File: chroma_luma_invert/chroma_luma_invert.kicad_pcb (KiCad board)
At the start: 2 copper layers, 100 x 100 mm, 69 parts, among them J1 rca, J2 rca, J3 Barrel_Jack, J4 Conn_01x12, SW1 SPDT, SW2 SPDT, U1 AD8044, U2 LM393, U3 CD4051, U4 LM317, U5 74HC4538, U6 CD4040, U7 74HC4538, U8 74HC4538

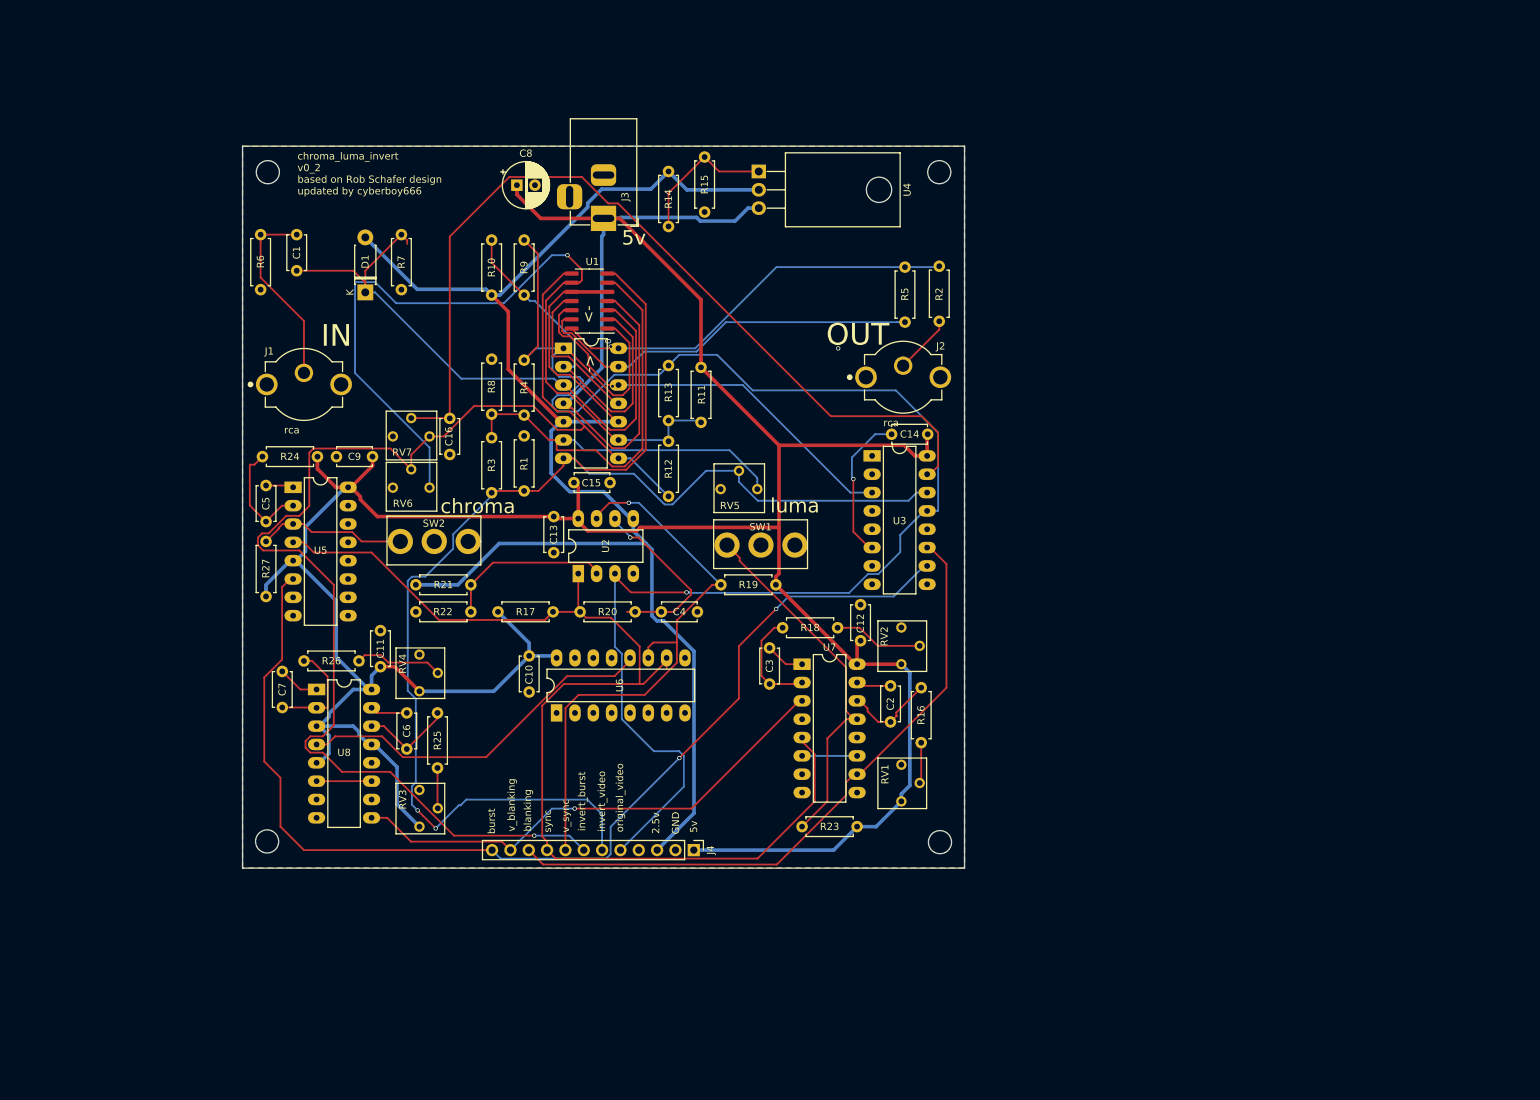
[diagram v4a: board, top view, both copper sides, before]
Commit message: update for new chroma_luma circuit
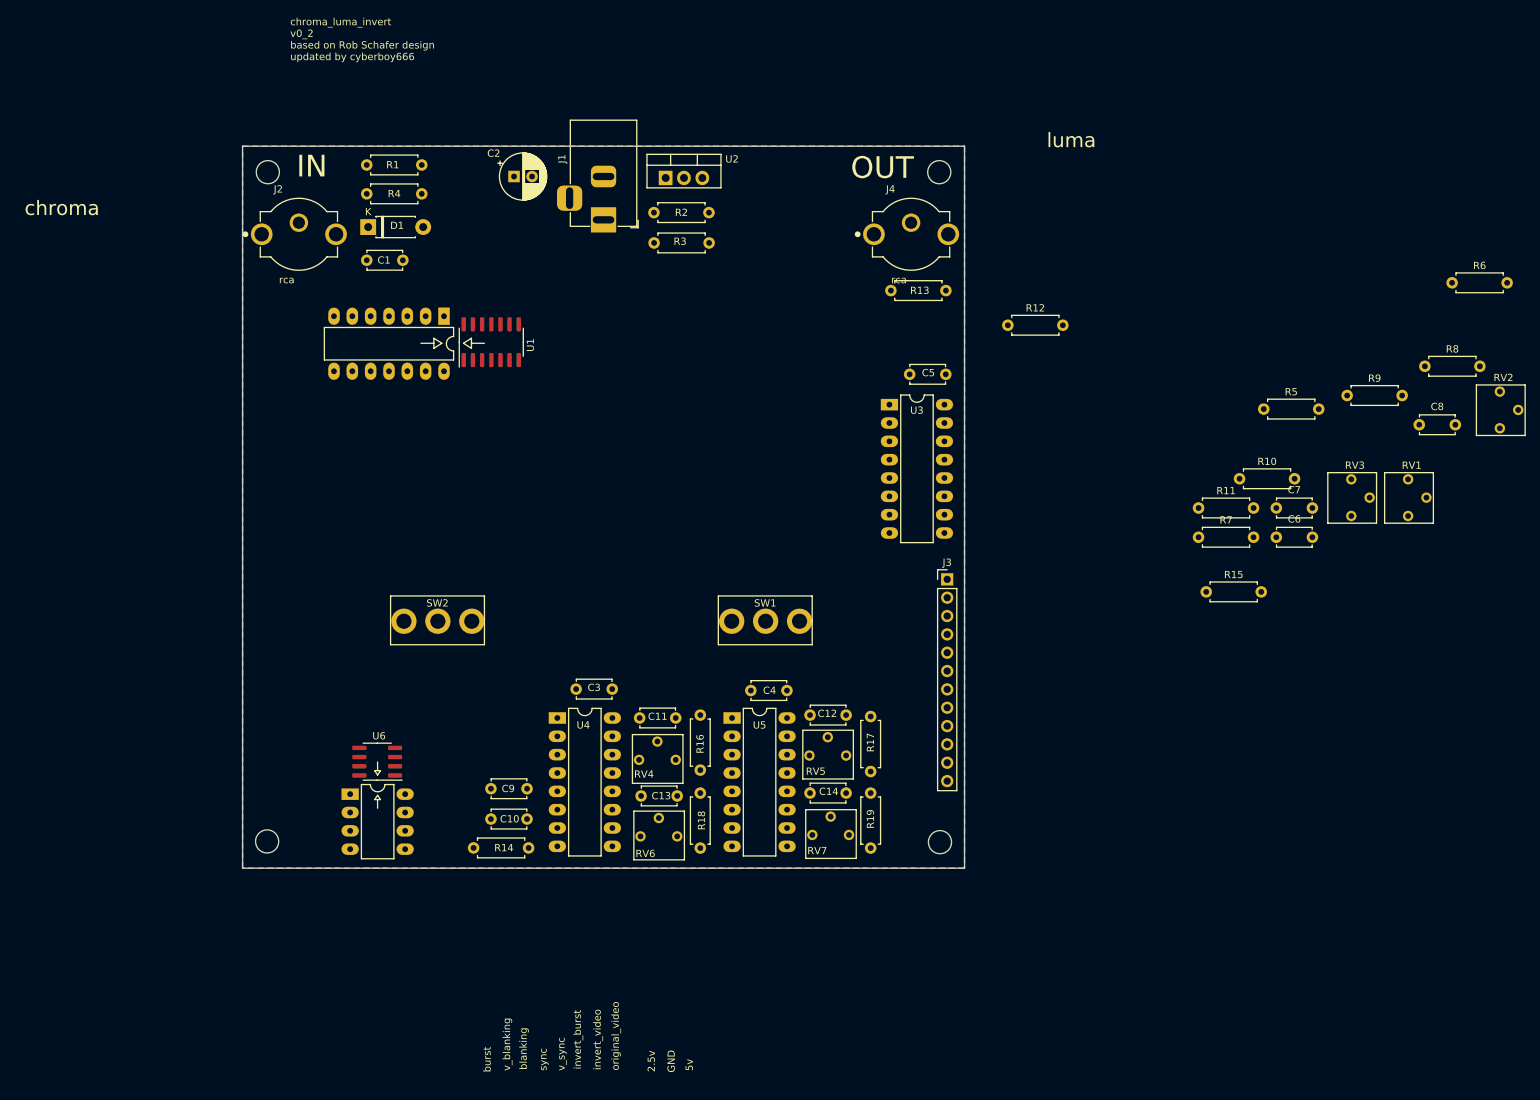
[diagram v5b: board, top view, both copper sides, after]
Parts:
- removed C15: 0.1u, Capacitor_THT:C_Disc_D4.7mm_W2.5mm_P5.00mm
- removed C16: 0.001u, Capacitor_THT:C_Disc_D4.7mm_W2.5mm_P5.00mm
- removed R20, R25: 15k, Resistor_THT:R_Axial_DIN0207_L6.3mm_D2.5mm_P7.62mm_Horizontal
- removed R21: 3.9k, Resistor_THT:R_Axial_DIN0207_L6.3mm_D2.5mm_P7.62mm_Horizontal
- removed R22, R23, R26, R27: 10k, Resistor_THT:R_Axial_DIN0207_L6.3mm_D2.5mm_P7.62mm_Horizontal
- removed R24: 39k, Resistor_THT:R_Axial_DIN0207_L6.3mm_D2.5mm_P7.62mm_Horizontal
- removed U7, U8: 74HC4538, Package_DIP:DIP-16_W7.62mm_LongPads
- C11: value 0.1u -> x1
- C12, C14: value 0.1u -> 0.001u
- C13: value 0.1u -> x2
- C2: value 0.001u -> 10uf; footprint Capacitor_THT:C_Disc_D4.7mm_W2.5mm_P5.00mm -> Capacitor_THT:CP_Radial_D6.3mm_P2.50mm
- C3, C4: value 0.001u -> 0.1u
- C5: value 0.0001u -> 0.1u
- C6, C7: value 0.01u -> 0.1u
- C8: value 10uf -> 0.001u; footprint Capacitor_THT:CP_Radial_D6.3mm_P2.50mm -> Capacitor_THT:C_Disc_D4.7mm_W2.5mm_P5.00mm
- J1: value rca -> Barrel_Jack; footprint lib_fp:tht_vertical_rca -> Connector_BarrelJack:BarrelJack_Horizontal
- J3: value Barrel_Jack -> Conn_01x12; footprint Connector_BarrelJack:BarrelJack_Horizontal -> Connector_PinHeader_2.54mm:PinHeader_1x12_P2.54mm_Vertical
- J4: value Conn_01x12 -> rca; footprint Connector_PinHeader_2.54mm:PinHeader_1x12_P2.54mm_Vertical -> lib_fp:tht_vertical_rca
- R1: value 1.5k -> 75
- R10: value 1k -> 5.6k
- R11: value 5.6k -> 1.5k
- R13: value 1k -> 75
- R14: value 100 -> 680k
- R15: value 100 -> 10k
- R16: value 68k -> y1
- R17: value 1k -> 10k
- R18: value 10k -> y2
- R19: value 1k -> 68k
- R2: value 75 -> 100
- R3: value 1.5k -> 100
- R4: value 1k -> 1m
- R6: value 75 -> 1k
- R7: value 1m -> 1k
- RV1: value 10k_trim -> 1k_trim
- RV2: value 5k_trim -> 1k_trim
- RV3: value 100k_trim -> 1k_trim
- RV4: value 20k_trim -> z1
- RV5: value 1k_trim -> 5k_trim
- RV6: value 1k_trim -> z2
- RV7: value 1k_trim -> 10k_trim
- U1: footprint project_parts:DIP+SOIC_14 -> lib_fp:DIP+SOIC_14
- U2: value LM393 -> LM317; footprint Package_DIP:DIP-8_W7.62mm_LongPads -> Package_TO_SOT_THT:TO-220-3_Vertical
- U4: value LM317 -> 74HC4538; footprint Package_TO_SOT_THT:TO-220-3_Horizontal_TabDown -> Package_DIP:DIP-16_W7.62mm_LongPads
- U6: value CD4040 -> LM1881; footprint Package_DIP:DIP-16_W7.62mm_LongPads -> lib_fp:DIP-SOIC-8
- moved R6 165.2 mm to (272.5, 53.9), turned to 0 degrees
- moved C7 139.5 mm to (248.2, 85.1), turned to 0 degrees
- moved RV3 136.1 mm to (258.6, 86.2)
- moved C8 129.3 mm to (268.0, 73.6)
- moved R8 129.3 mm to (268.8, 65.5), turned to 0 degrees
- moved C6 122.9 mm to (248.2, 89.2), turned to 0 degrees
- moved R7 118.1 mm to (237.4, 89.2), turned to 0 degrees
- moved R9 116.0 mm to (258.0, 69.5), turned to 0 degrees
- moved R10 108.7 mm to (243.1, 81.1), turned to 0 degrees
- moved R14 97.5 mm to (137.0, 132.2), turned to 0 degrees
- moved R15 92.0 mm to (238.5, 96.7), turned to 0 degrees
- moved C5 90.5 mm to (197.4, 66.6), turned to 0 degrees
- moved J4 90.5 mm to (197.6, 47.2), turned to 0 degrees
- moved RV2 89.1 mm to (279.2, 74.1)
- moved C2 87.7 mm to (142.6, 39.2), turned to 0 degrees
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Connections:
- C10 pad 1: GND -> Net-(C10-Pad1)
- C10 pad 2: +5V -> GND
- C11 pad 1: GND -> Net-(C11-Pad1)
- C11 pad 2: +5V -> Net-(C11-Pad2)
- C12 pad 1: GND -> Net-(C12-Pad1)
- C12 pad 2: +5V -> Net-(C12-Pad2)
- C13 pad 1: GND -> Net-(C13-Pad1)
- C13 pad 2: +5V -> Net-(C13-Pad2)
- C14 pad 1: GND -> Net-(C14-Pad1)
- C14 pad 2: +5V -> Net-(C14-Pad2)
- C2 pad 1: Net-(C2-Pad1) -> +5V
- C2 pad 2: Net-(C2-Pad2) -> GND
- C3 pad 1: Net-(C3-Pad1) -> GND
- C3 pad 2: Net-(C3-Pad2) -> +5V
- C4 pad 2: Net-(C4-Pad2) -> +5V
- C5 pad 1: Net-(C5-Pad1) -> GND
- C5 pad 2: Net-(C5-Pad2) -> +5V
- C6 pad 1: Net-(C6-Pad1) -> GND
- C6 pad 2: Net-(C6-Pad2) -> +5V
- C7 pad 1: Net-(C7-Pad1) -> GND
- C7 pad 2: Net-(C7-Pad2) -> +5V
- C8 pad 1: +5V -> Net-(C8-Pad1)
- C9 pad 1: GND -> Net-(C9-Pad1)
- C9 pad 2: +5V -> original_video
- J1 pad 1: Net-(C1-Pad2) -> +5V
- J2 pad 1: Net-(J2-Pad1) -> Net-(C1-Pad2)
- J3 pad 3: GND -> 2.5V
- J4 pad 1: +5V -> Net-(J4-Pad1)
- R1 pad 1: invert_video -> Net-(C1-Pad2)
- R1 pad 2: Net-(R1-Pad2) -> GND
- R10 pad 2: 2.5V -> +5V
- R11 pad 1: Net-(R11-Pad1) -> invert_video
- R11 pad 2: +5V -> Net-(R11-Pad2)
- R12 pad 1: invert_burst -> Net-(R12-Pad1)
- R12 pad 2: Net-(R11-Pad1) -> Net-(R12-Pad2)
- R13 pad 1: Net-(R11-Pad1) -> Net-(J4-Pad1)
- R13 pad 2: original_video -> Net-(R12-Pad1)
- R14 pad 1: 2.5V -> GND
- R14 pad 2: Net-(R14-Pad2) -> Net-(C10-Pad1)
- R15 pad 1: Net-(R14-Pad2) -> /blanking_and_burst/blanking_enable
- R15 pad 2: GND -> +5V
- R16 pad 1: Net-(C2-Pad2) -> Net-(C11-Pad2)
- R17 pad 1: sync -> Net-(C12-Pad2)
- R17 pad 2: +5V -> Net-(R17-Pad2)
- R18 pad 1: Net-(C3-Pad2) -> Net-(C13-Pad2)
- R19 pad 1: v_sync -> Net-(C14-Pad2)
- R19 pad 2: +5V -> Net-(R19-Pad2)
- R2 pad 1: Net-(J2-Pad1) -> 2.5V
- R3 pad 1: invert_video -> Net-(R2-Pad2)
- R3 pad 2: Net-(R3-Pad2) -> GND
- R4 pad 1: Net-(R3-Pad2) -> Net-(C1-Pad1)
- R4 pad 2: original_video -> GND
- R5 pad 1: Net-(R2-Pad2) -> Net-(R5-Pad1)
- R5 pad 2: Net-(R5-Pad2) -> 2.5V
- R6 pad 1: Net-(C1-Pad2) -> original_video
- R6 pad 2: GND -> Net-(R5-Pad1)
- R7 pad 1: Net-(C1-Pad1) -> Net-(R11-Pad2)
- R7 pad 2: GND -> original_video
- R8 pad 2: Net-(R3-Pad2) -> Net-(R11-Pad2)
- R9 pad 1: original_video -> Net-(R10-Pad1)
- R9 pad 2: Net-(R10-Pad1) -> original_video
- RV1 pad 1: +5V -> Net-(R10-Pad1)
- RV1 pad 2: Net-(R16-Pad2) -> invert_burst
- RV2 pad 1: +5V -> Net-(R11-Pad2)
- RV2 pad 2: Net-(R18-Pad2) -> invert_video
- RV3 pad 1: +5V -> invert_burst
- RV3 pad 2: Net-(R25-Pad2) -> Net-(C8-Pad1)
- RV4 pad 2: Net-(R26-Pad2) -> Net-(R16-Pad2)
- RV5 pad 1: Net-(R3-Pad2) -> +5V
- RV5 pad 2: invert_video -> Net-(R17-Pad2)
- RV6 pad 1: Net-(R11-Pad1) -> +5V
- RV6 pad 2: invert_burst -> Net-(R18-Pad2)
- RV7 pad 1: invert_burst -> +5V
- RV7 pad 2: Net-(C16-Pad1) -> Net-(R19-Pad2)
- SW2 pad 1: /blanking_and_burst/burst_enable -> burst_pulse
- U1 pad 13: Net-(R5-Pad2) -> Net-(R12-Pad2)
- U1 pad 14: Net-(R2-Pad2) -> Net-(R12-Pad1)
- U1 pad 2: Net-(R10-Pad1) -> Net-(R5-Pad1)
- U1 pad 6: Net-(R3-Pad2) -> Net-(R11-Pad2)
- U1 pad 9: Net-(R11-Pad1) -> Net-(R10-Pad1)
- U2 pad 1: sync -> Net-(R2-Pad2)
- U2 pad 2: Net-(R21-Pad2) -> 2.5V
- U2 pad 3: original_video -> +5V
- U3 pad 15: Net-(C16-Pad1) -> Net-(C8-Pad1)
- U4 pad 1: Net-(R14-Pad2) -> Net-(C11-Pad1)
- U4 pad 2: 2.5V -> Net-(C11-Pad2)
- U5 pad 1: Net-(C5-Pad1) -> Net-(C12-Pad1)
- U5 pad 10: (no net) -> blanking
- U5 pad 11: (no net) -> Net-(U5-Pad11)
- U5 pad 12: (no net) -> GND
- U5 pad 13: (no net) -> /blanking_and_burst/blanking_enable
- U5 pad 14: (no net) -> Net-(C14-Pad2)
- U5 pad 15: (no net) -> Net-(C14-Pad1)
- U5 pad 2: Net-(C5-Pad2) -> Net-(C12-Pad2)
- U5 pad 3: /blanking_and_burst/burst_enable -> v_blanking
- U5 pad 4: sync -> GND
- U5 pad 5: +5V -> sync
- U5 pad 6: burst_pulse -> Net-(U5-Pad11)
- U5 pad 9: (no net) -> Net-(U5-Pad9)
- U6 pad 1: Net-(U6-Pad1) -> sync
- U6 pad 2: Net-(U6-Pad2) -> Net-(C9-Pad1)
- U6 pad 3: Net-(U6-Pad3) -> v_sync
- U6 pad 4: Net-(U6-Pad4) -> GND
- U6 pad 5: Net-(U6-Pad5) -> burst_pulse
- U6 pad 6: Net-(U6-Pad6) -> Net-(C10-Pad1)
- U6 pad 8: GND -> +5V
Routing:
- net +5V: track 466.5 -> 0.00 mm
- net original_video: track 234.1 -> 0.00 mm, vias 1 -> 0
- net 2.5V: track 234.1 -> 0.00 mm
- net invert_video: track 200.3 -> 0.00 mm, vias 2 -> 0
- net invert_burst: track 188.2 -> 0.00 mm, vias 1 -> 0
- net sync: track 158.3 -> 0.00 mm
- net burst_pulse: track 151.8 -> 0.00 mm, vias 2 -> 0
- net Net-(C16-Pad1): track 122.9 -> 0.00 mm
- net Net-(R11-Pad1): track 115.7 -> 0.00 mm, vias 1 -> 0
- net blanking: track 90.6 -> 0.00 mm
- net Net-(R3-Pad2): track 86.7 -> 0.00 mm
- net Net-(C1-Pad1): track 86.6 -> 0.00 mm
- net v_sync: track 82.0 -> 0.00 mm, vias 1 -> 0
- net v_blanking: track 70.0 -> 0.00 mm, vias 1 -> 0
- net Net-(U1-Pad12): track 57.9 -> 0.00 mm, vias 2 -> 0
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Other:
- board text removed: "<-"

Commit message: working on nexr version for colorizer and inverter
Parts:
- removed C8: 0.001u, Capacitor_THT:C_Disc_D4.7mm_W2.5mm_P5.00mm
- removed the REF** at (201.5, 38.6)
- removed the REF** at (201.6, 131.4)
- removed the REF** at (108.4, 131.3)
- removed the REF** at (108.5, 38.6)
- added R20: ??10k, Resistor_THT:R_Axial_DIN0207_L6.3mm_D2.5mm_P7.62mm_Horizontal, F.Cu at (160.5, 91.4)
- added R21: ??10k, Resistor_THT:R_Axial_DIN0207_L6.3mm_D2.5mm_P7.62mm_Horizontal, F.Cu at (160.5, 95.5)
- added R22: 1k, Resistor_THT:R_Axial_DIN0207_L6.3mm_D2.5mm_P7.62mm_Horizontal, F.Cu at (141.7, 82.8)
- added R23: 5k, Resistor_THT:R_Axial_DIN0207_L6.3mm_D2.5mm_P7.62mm_Horizontal, F.Cu at (116.8, 71.6)
- added R24: ??not connected, Resistor_THT:R_Axial_DIN0207_L6.3mm_D2.5mm_P7.62mm_Horizontal, F.Cu at (168.1, 86.9)
- added R25: 1.5k, Resistor_THT:R_Axial_DIN0207_L6.3mm_D2.5mm_P7.62mm_Horizontal, F.Cu at (141.7, 86.9)
- added R26: ??1.5k, Resistor_THT:R_Axial_DIN0207_L6.3mm_D2.5mm_P7.62mm_Horizontal, F.Cu at (160.5, 82.8)
- added REF**: MountingHole_3.2mm_M3, MountingHole:MountingHole_3.2mm_M3, F.Cu at (108.7, 131.6)
- added REF**: MountingHole_3.2mm_M3, MountingHole:MountingHole_3.2mm_M3, F.Cu at (201.7, 131.6)
- added REF**: MountingHole_3.2mm_M3, MountingHole:MountingHole_3.2mm_M3, F.Cu at (201.7, 38.6)
- added REF**: MountingHole_3.2mm_M3, MountingHole:MountingHole_3.2mm_M3, F.Cu at (108.7, 38.6)
- added RV8: ??20k_trim, lib_fp:tht_vertical_trimpot_3362, F.Cu at (121.9, 77.7)
- C11: value x1 -> 0.1uf
- C13: value x2 -> 1uf
- R10: value 5.6k -> ??10k
- R11: value 1.5k -> 1k
- R16: value y1 -> 12k
- R18: value y2 -> 22k
- R7: value 1k -> ??k
- R8: value 2.2k -> ??k
- R9: value 1k -> ??10k
- RV1: value 1k_trim -> ??k_trim
- RV2, RV3: value 1k_trim -> ??100k_pot; footprint lib_fp:tht_vertical_trimpot_3362 -> lib_fp:Potentiometer_Vertical_Large
- RV4: value z1 -> 10k_trim
- RV6: value z2 -> 10k_trim
- SW1, SW2: footprint lib_fp:mini_toggle_switch_tayda -> lib_fp:spdt_slide_switch_small_tayda
- moved R8 157.0 mm to (114.8, 96.0)
- moved RV1 144.5 mm to (121.9, 85.9), turned to 90 degrees
- moved R6 138.5 mm to (134.1, 50.8)
- moved C7 130.0 mm to (121.4, 113.8), turned to 180 degrees
- moved RV3 124.0 mm to (134.6, 87.4), turned to 90 degrees
- moved R7 122.6 mm to (114.8, 91.9)
- moved R11 121.8 mm to (116.8, 67.6)
- moved R9 118.3 mm to (141.7, 91.4)
- moved R15 115.2 mm to (124.0, 109.2), turned to 180 degrees
- moved R5 107.7 mm to (141.7, 46.2), turned to 180 degrees
- moved R10 102.4 mm to (141.7, 95.5)
- moved RV2 100.2 mm to (179.8, 87.4), turned to 90 degrees
- moved C6 87.8 mm to (167.1, 55.4), turned to 180 degrees
- moved U1 21.0 mm to (155.4, 59.9), turned to 0 degrees
- moved C9 19.3 mm to (128.0, 113.8), turned to 90 degrees
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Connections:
- R10 pad 2: +5V -> Net-(R10-Pad2)
- R11 pad 1: invert_video -> Net-(R11-Pad1)
- R11 pad 2: Net-(R11-Pad2) -> original_video
- R7 pad 1: Net-(R11-Pad2) -> Net-(R7-Pad1)
- R7 pad 2: original_video -> +5V
- R8 pad 2: Net-(R11-Pad2) -> Net-(R8-Pad2)
- RV1 pad 1: Net-(R10-Pad1) -> Net-(R7-Pad1)
- RV1 pad 2: invert_burst -> Net-(R10-Pad2)
- RV1 pad 3: Net-(RV1-Pad3) -> Net-(R8-Pad2)
- RV2 pad 1: Net-(R11-Pad2) -> original_video
- RV2 pad 2: invert_video -> Net-(R10-Pad1)
- RV2 pad 3: Net-(RV2-Pad3) -> Net-(R10-Pad2)
- RV3 pad 1: invert_burst -> original_video
- RV3 pad 2: Net-(C8-Pad1) -> Net-(R20-Pad1)
- RV3 pad 3: Net-(RV3-Pad3) -> 2.5V
- U1 pad 10: 2.5V -> Net-(R20-Pad1)
- U1 pad 5: 2.5V -> Net-(R10-Pad1)
- U1 pad 6: Net-(R11-Pad2) -> Net-(R11-Pad1)
- U1 pad 9: Net-(R10-Pad1) -> Net-(R22-Pad1)
- U3 pad 15: Net-(C8-Pad1) -> invert_burst
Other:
- board text added: "chroma_luma_invert v0_3 based on Rob Schafer design updated by cyberboy666"
- board text removed: "chroma_luma_invert v0_2 based on Rob Schafer design updated by cyberboy666"

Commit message: newest circuit revisions
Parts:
- removed C14: 0.001u, Capacitor_THT:C_Disc_D4.7mm_W2.5mm_P5.00mm
- removed the REF** at (108.7, 131.6)
- removed the REF** at (201.7, 131.6)
- removed the REF** at (201.7, 38.6)
- removed the REF** at (108.7, 38.6)
- added C8: 0.1u, Capacitor_THT:C_Disc_D4.7mm_W2.5mm_P5.00mm, F.Cu at (108.8, 99.5)
- added J5: Conn_02x08_Odd_Even, Connector_PinHeader_2.54mm:PinHeader_2x08_P2.54mm_Vertical, F.Cu at (191.0, 37.4)
- added REF**: MountingHole_3.2mm_M3, MountingHole:MountingHole_3.2mm_M3, F.Cu at (201.5, 38.5)
- added REF**: MountingHole_3.2mm_M3, MountingHole:MountingHole_3.2mm_M3, F.Cu at (201.5, 131.5)
- added REF**: MountingHole_3.2mm_M3, MountingHole:MountingHole_3.2mm_M3, F.Cu at (108.5, 131.5)
- added REF**: MountingHole_3.2mm_M3, MountingHole:MountingHole_3.2mm_M3, F.Cu at (108.4, 38.5)
- C10: value 0.1u -> 0.1uf
- C11: value 0.1uf -> 0.001u
- C12: value 0.001u -> 1uf
- C13: value 1uf -> 0.001u
- R10: value ??10k -> 10k
- R11: value 1k -> 12k
- R12: value 1k -> 10k
- R13: value 75 -> 22k
- R14: value 680k -> 68k
- R15: value 10k -> ??k
- R16: value 12k -> ??k
- R17: value 10k -> ??10k
- R18: value 22k -> ??10k
- R19: value 68k -> 1k
- R7: value ??k -> 1k
- R8: value ??k -> 75
- R9: value ??10k -> 680k
- RV1: value ??k_trim -> 10k_trim
- RV2: value ??100k_pot -> 5k_trim; footprint lib_fp:Potentiometer_Vertical_Large -> lib_fp:tht_vertical_trimpot_3362
- RV3: value ??100k_pot -> 10k_trim; footprint lib_fp:Potentiometer_Vertical_Large -> lib_fp:tht_vertical_trimpot_3362
- RV5: value 5k_trim -> ??k_trim
- RV6, RV7: value 10k_trim -> ??100k_pot; footprint lib_fp:tht_vertical_trimpot_3362 -> lib_fp:Potentiometer_Vertical_Large
- moved R13 97.2 mm to (136.4, 132.6), turned to 90 degrees
- moved R8 88.3 mm to (187.4, 45.7), turned to 180 degrees
- moved C5 84.2 mm to (127.7, 110.5)
- moved C3 83.2 mm to (196.3, 54.5)
- moved R7 68.4 mm to (173.7, 57.0)
- moved RV7 68.3 mm to (132.9, 84.9)
- moved C6 66.4 mm to (125.3, 107.0)
- moved R19 65.2 mm to (173.5, 69.9), turned to 0 degrees
- moved R23 64.6 mm to (181.2, 65.5), turned to 180 degrees
- moved R12 60.6 mm to (174.9, 113.2), turned to 270 degrees
- moved R11 57.6 mm to (136.4, 121.8), turned to 90 degrees
- moved RV6 54.1 mm to (181.8, 85.1)
- moved RV8 50.0 mm to (170.0, 91.6)
- moved R14 47.7 mm to (174.9, 124.4), turned to 270 degrees
- moved R10 47.3 mm to (188.6, 88.6), turned to 270 degrees
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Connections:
- C10 pad 2: GND -> Net-(C10-Pad2)
- C9 pad 2: original_video -> GND
- R10 pad 1: Net-(R10-Pad1) -> /blanking_and_burst/blanking_enable
- R10 pad 2: Net-(R10-Pad2) -> +5V
- R11 pad 1: Net-(R11-Pad1) -> Net-(C10-Pad2)
- R11 pad 2: original_video -> Net-(R11-Pad2)
- R12 pad 1: Net-(R12-Pad1) -> Net-(C11-Pad2)
- R13 pad 1: Net-(J4-Pad1) -> Net-(C12-Pad2)
- R13 pad 2: Net-(R12-Pad1) -> Net-(R13-Pad2)
- R14 pad 1: GND -> Net-(C13-Pad2)
- R14 pad 2: Net-(C10-Pad1) -> Net-(R14-Pad2)
- R15 pad 1: /blanking_and_burst/blanking_enable -> Net-(R15-Pad1)
- R16 pad 1: Net-(C11-Pad2) -> GND
- R17 pad 1: Net-(C12-Pad2) -> Net-(R17-Pad1)
- R17 pad 2: Net-(R17-Pad2) -> original_video
- R18 pad 1: Net-(C13-Pad2) -> Net-(R17-Pad1)
- R19 pad 1: Net-(C14-Pad2) -> Net-(R19-Pad1)
- R19 pad 2: Net-(R19-Pad2) -> original_video
- R23 pad 1: Net-(R11-Pad1) -> Net-(R19-Pad1)
- R25 pad 2: Net-(R11-Pad1) -> Net-(R19-Pad1)
- R7 pad 2: +5V -> Net-(R7-Pad2)
- R8 pad 1: GND -> Net-(J4-Pad1)
- R8 pad 2: Net-(R8-Pad2) -> Net-(R7-Pad1)
- R9 pad 1: Net-(R10-Pad1) -> GND
- R9 pad 2: original_video -> Net-(C9-Pad1)
- RV1 pad 1: Net-(R7-Pad1) -> +5V
- RV1 pad 2: Net-(R10-Pad2) -> Net-(R11-Pad2)
- RV1 pad 3: Net-(R8-Pad2) -> Net-(RV1-Pad3)
- RV2 pad 1: original_video -> +5V
- RV2 pad 2: Net-(R10-Pad1) -> Net-(R12-Pad2)
- RV2 pad 3: Net-(R10-Pad2) -> Net-(RV2-Pad3)
- RV3 pad 1: original_video -> +5V
- RV3 pad 2: Net-(R20-Pad1) -> Net-(R13-Pad2)
- RV3 pad 3: 2.5V -> Net-(RV3-Pad3)
- RV4 pad 2: Net-(R16-Pad2) -> Net-(R14-Pad2)
- RV5 pad 1: +5V -> Net-(R15-Pad1)
- RV5 pad 2: Net-(R17-Pad2) -> Net-(R18-Pad2)
- RV5 pad 3: Net-(RV5-Pad3) -> Net-(R16-Pad2)
- RV6 pad 1: +5V -> original_video
- RV6 pad 2: Net-(R18-Pad2) -> Net-(R17-Pad1)
- RV6 pad 3: Net-(RV6-Pad3) -> Net-(R18-Pad2)
- RV7 pad 1: +5V -> original_video
- RV7 pad 2: Net-(R19-Pad2) -> Net-(R20-Pad1)
- RV7 pad 3: Net-(RV7-Pad3) -> 2.5V
- U1 pad 13: Net-(R12-Pad2) -> Net-(R7-Pad2)
- U1 pad 14: Net-(R12-Pad1) -> Net-(R7-Pad1)
- U1 pad 5: Net-(R10-Pad1) -> Net-(R17-Pad1)
- U1 pad 6: Net-(R11-Pad1) -> Net-(R19-Pad1)
- U4 pad 1: Net-(C11-Pad1) -> Net-(C10-Pad1)
- U4 pad 14: Net-(C13-Pad2) -> Net-(C12-Pad2)
- U4 pad 15: Net-(C13-Pad1) -> Net-(C12-Pad1)
- U4 pad 2: Net-(C11-Pad2) -> Net-(C10-Pad2)
- U5 pad 1: Net-(C12-Pad1) -> Net-(C11-Pad1)
- U5 pad 14: Net-(C14-Pad2) -> Net-(C13-Pad2)
- U5 pad 15: Net-(C14-Pad1) -> Net-(C13-Pad1)
- U5 pad 2: Net-(C12-Pad2) -> Net-(C11-Pad2)
- U6 pad 2: Net-(C9-Pad1) -> Net-(C8-Pad1)
- U6 pad 6: Net-(C10-Pad1) -> Net-(C9-Pad1)
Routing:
- net +5V: track 0.00 -> 421.4 mm
- net 2.5V: track 0.00 -> 226.9 mm, vias 0 -> 1
- net original_video: track 0.00 -> 223.2 mm, vias 0 -> 1
- net burst_pulse: track 0.00 -> 181.5 mm, vias 0 -> 2
- net invert_burst: track 0.00 -> 172.7 mm, vias 0 -> 1
- net sync: track 0.00 -> 139.3 mm, vias 0 -> 2
- net invert_video: track 0.00 -> 122.5 mm
- net v_sync: track 0.00 -> 115.5 mm
- net Net-(R22-Pad1): track 0.00 -> 104.8 mm
- net Net-(R19-Pad1): track 0.00 -> 90.8 mm
- net v_blanking: track 0.00 -> 89.5 mm
- net Net-(R20-Pad1): track 0.00 -> 86.7 mm, vias 0 -> 1
- net blanking: track 0.00 -> 84.8 mm, vias 0 -> 1
- net Net-(R17-Pad1): track 0.00 -> 81.9 mm
- net GND: track 0.00 -> 72.5 mm, vias 0 -> 5
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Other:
- board text added: "n"
- board text added: "p"

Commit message: updates
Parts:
- C11, C13: value 0.001u -> 1n
- R11: value 12k -> 18k
- R14: value 68k -> 75k
- R23: value 5k -> 5.1k
